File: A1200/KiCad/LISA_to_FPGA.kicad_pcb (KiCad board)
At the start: 4 copper layers, 64 x 37 mm, 30 parts, among them J1 Conn_01x01, J2 Conn_01x40, U1 LM1117-3.3, U2 74LVC162244ADGG, U3 74LVC162244ADGG, U4 LISA, U5 RP2354B

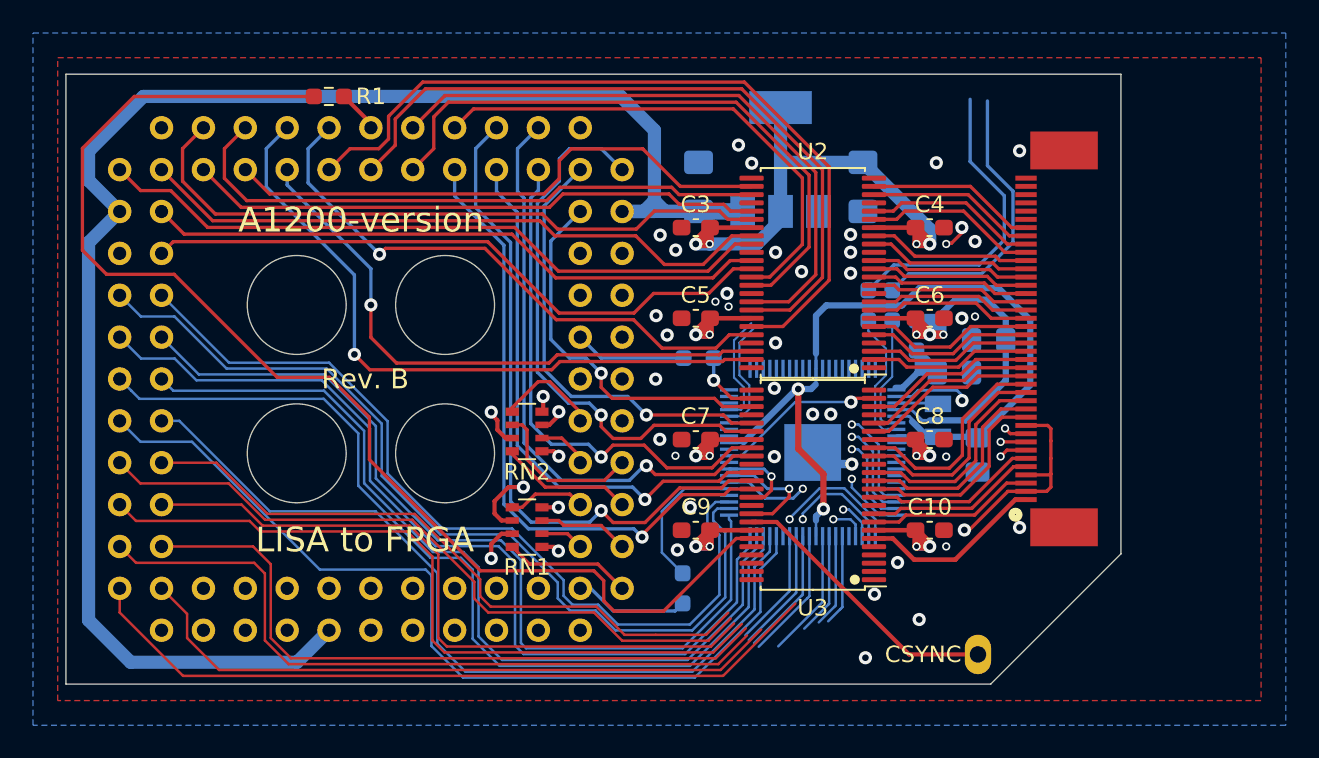
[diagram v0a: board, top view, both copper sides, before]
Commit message: Add 330 Ohm resistor pack RN3 and route D31-D28 to RP2354B
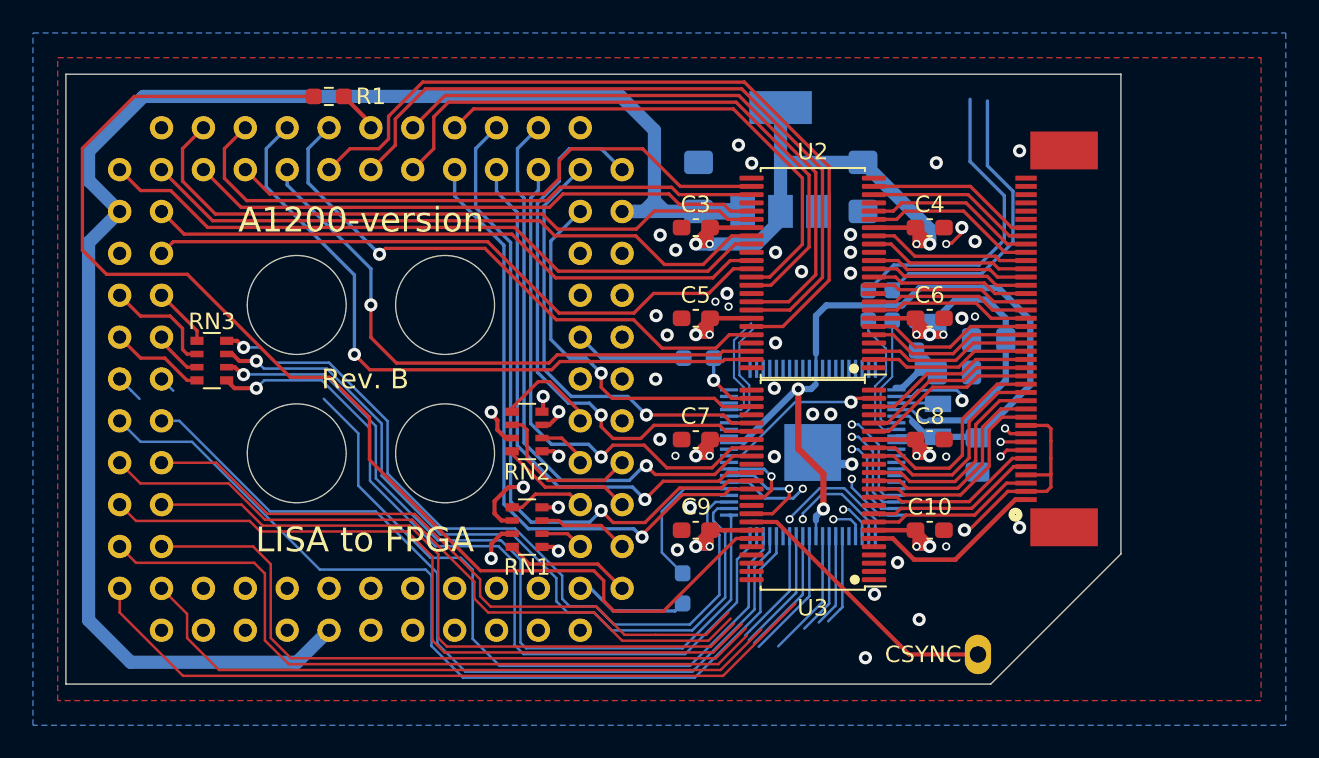
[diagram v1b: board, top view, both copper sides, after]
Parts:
- added RN3: R_Pack04, Resistor_SMD:R_Array_Convex_4x0603, F.Cu at (157.1, 89.3)
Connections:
- net /RGA11 renamed /RGA01
- net /RGA22 renamed /RGA02
- net /RGA33 renamed RGA03
- net /RGA44 renamed /RGA04
- net /RGA55 renamed /RGA05
- net /RGA66 renamed RGA06
- net /RGA77 renamed RGA07
- net /RGA88 renamed /RGA08
- U4 pad 59: D31 -> D031
- U4 pad 60: D30 -> D030
- U4 pad 61: D29 -> D029
- U4 pad 62: D28 -> D028
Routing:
- net D27: track 52.5 -> 1.01 mm
- net D26: track 55.8 -> 44.6 mm
- net D30: track 54.9 -> 47.2 mm, vias 0 -> 1
- net D28: track 55.9 -> 48.7 mm, vias 0 -> 1
- net D030: track 0.00 -> 6.92 mm
- net D028: track 0.00 -> 5.78 mm
- net D31: track 52.2 -> 47.4 mm, vias 0 -> 1
- net D29: track 53.6 -> 49.2 mm, vias 0 -> 1
- net D031: track 0.00 -> 3.65 mm
- net D029: track 0.00 -> 3.07 mm

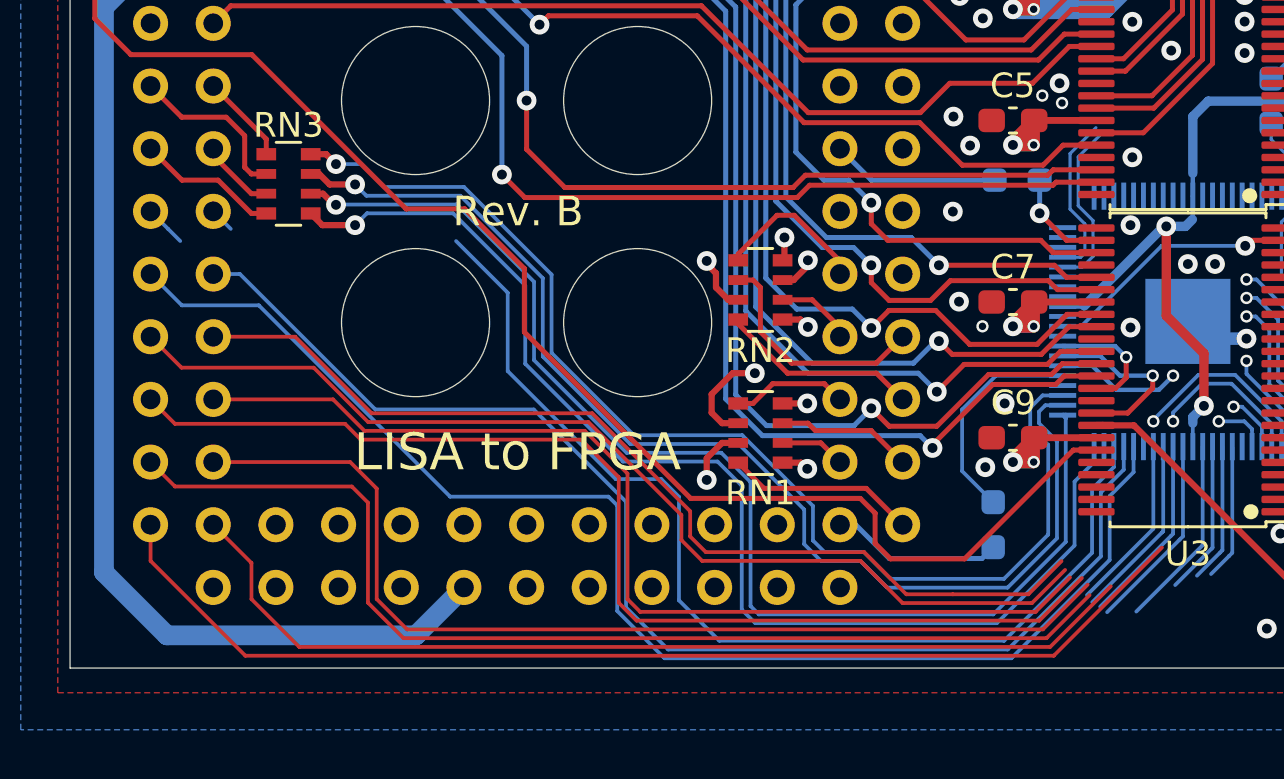
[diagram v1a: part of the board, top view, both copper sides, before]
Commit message: Add RN4 resistor pack and route D27-D24
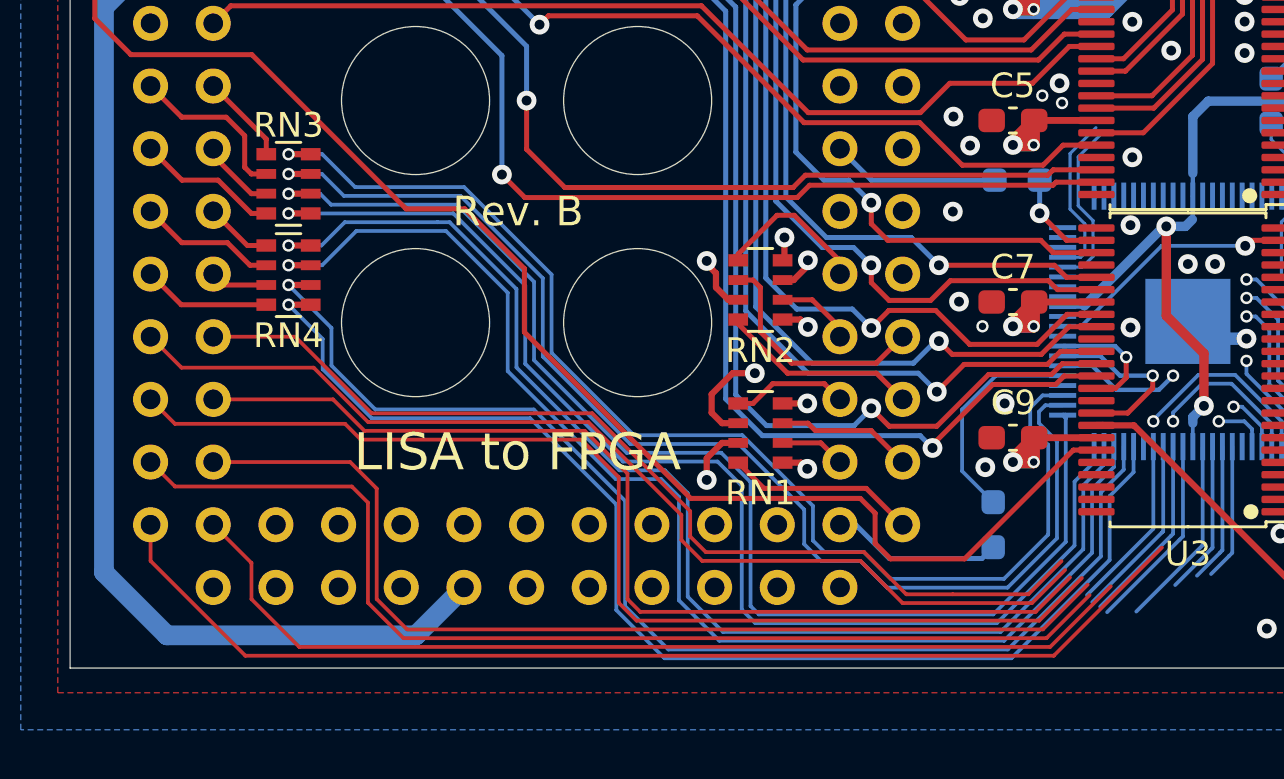
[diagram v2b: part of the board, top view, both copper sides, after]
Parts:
- added RN4: R_Pack04, Resistor_SMD:R_Array_Convex_4x0603, F.Cu at (157.1, 93.0)
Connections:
- net D028 renamed DQ28
- net D029 renamed DQ29
- net D030 renamed DQ30
- net D031 renamed DQ31
- U4 pad 63: D27 -> DQ27
- U4 pad 64: D26 -> DQ26
- U4 pad 65: D25 -> DQ25
- U4 pad 66: D24 -> DQ24
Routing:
- net D27: track 1.01 -> 50.6 mm, vias 0 -> 1
- net D26: track 44.6 -> 51.4 mm, vias 0 -> 1
- net DQ26: track 0.00 -> 5.59 mm
- net DQ24: track 0.00 -> 5.21 mm
- net D24: track 54.5 -> 50.0 mm, vias 0 -> 1
- net DQ27: track 0.00 -> 2.72 mm
- net DQ25: track 0.00 -> 2.33 mm
- net D30: track 47.2 -> 49.0 mm
- net D31: track 47.4 -> 49.2 mm
- net D29: track 49.2 -> 50.9 mm
- net D25: track 51.2 -> 49.7 mm, vias 0 -> 1
- net D28: track 48.7 -> 50.1 mm

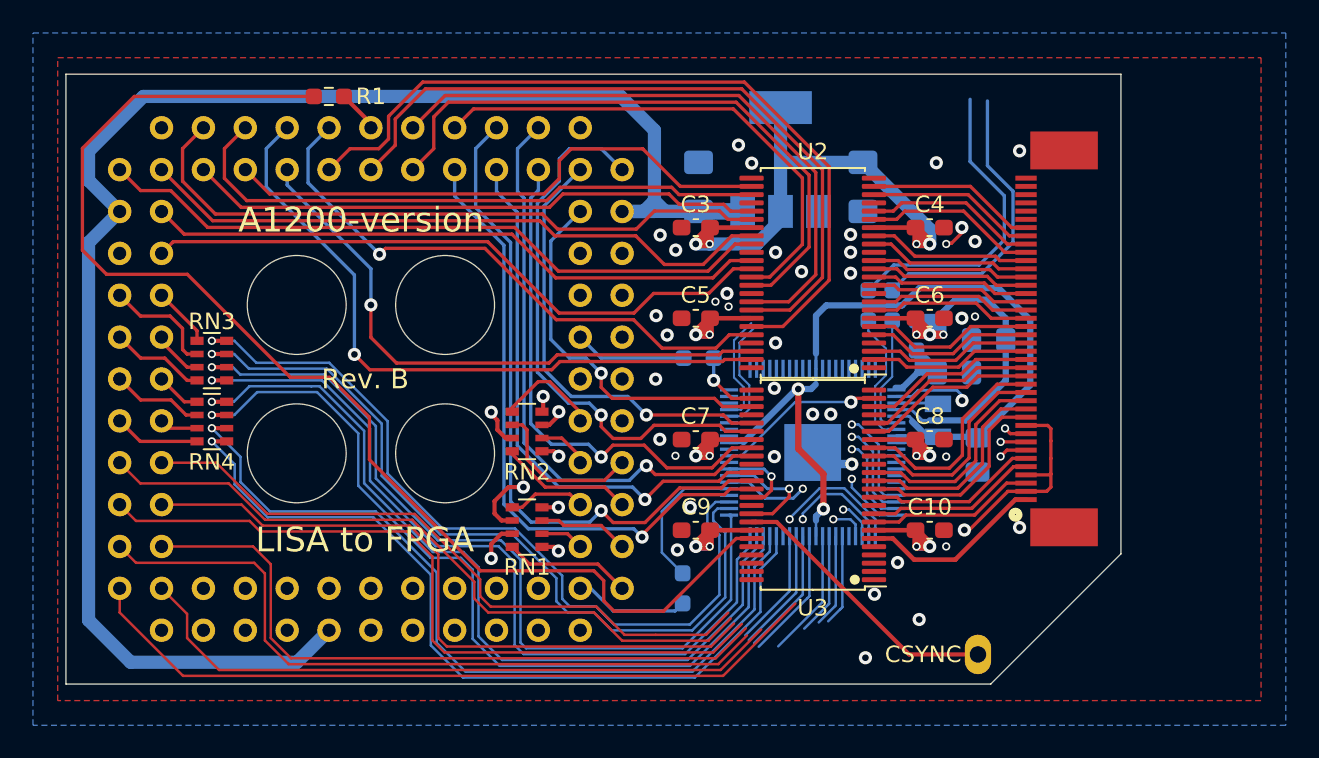
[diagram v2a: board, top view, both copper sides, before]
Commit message: Add RN5 resistor pack and route D23-D20
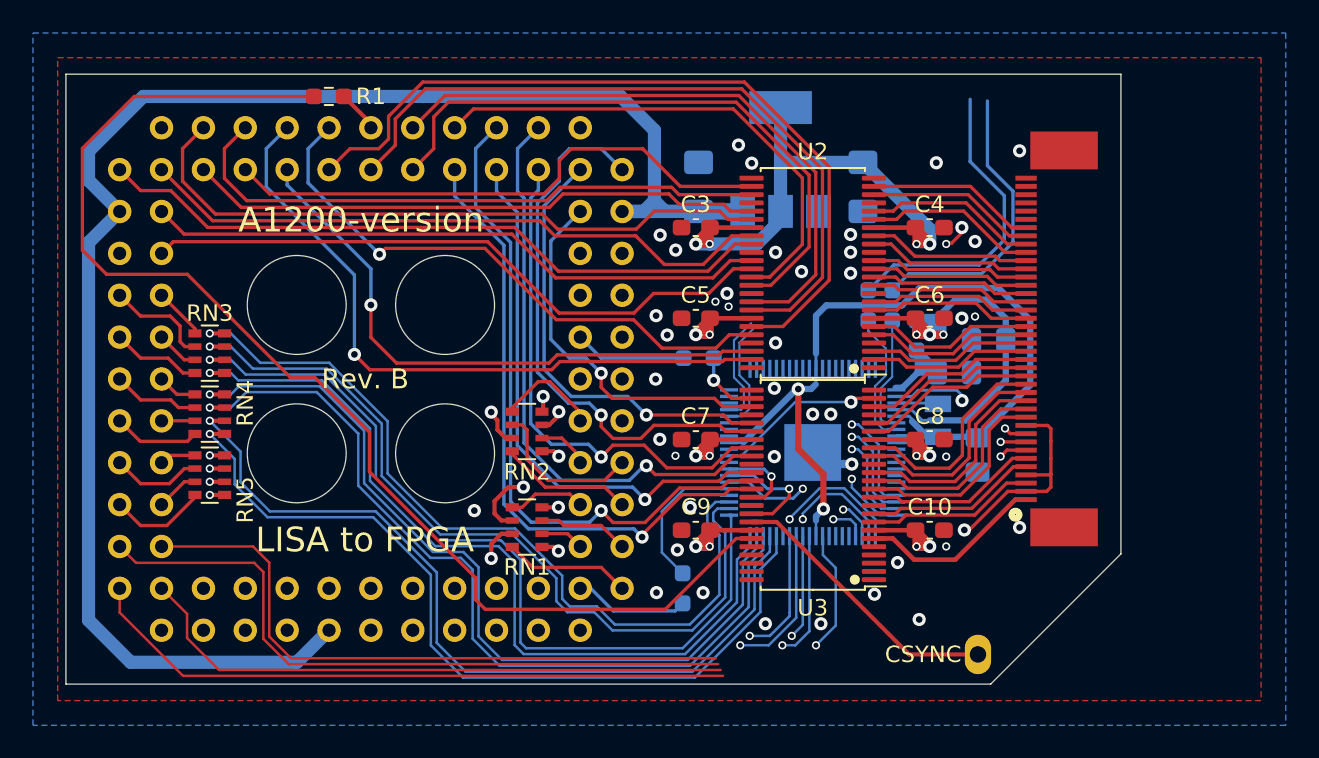
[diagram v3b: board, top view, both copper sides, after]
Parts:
- added RN5: R_Pack04, Resistor_SMD:R_Array_Convex_4x0603, F.Cu at (157.0, 96.3)
- moved RN3 0.47 mm to (157.0, 88.9)
- moved RN4 0.47 mm to (157.0, 92.6)
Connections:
- U4 pad 67: D23 -> DQ23
- U4 pad 68: D22 -> DQ22
- U4 pad 69: D21 -> DQ21
- U4 pad 70: D20 -> DQ20
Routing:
- net D16: track 51.4 -> 39.7 mm
- net D17: track 46.0 -> 36.8 mm
- net D18: track 50.4 -> 41.6 mm
- net DQ20: track 0.00 -> 5.95 mm
- net DQ22: track 0.00 -> 5.47 mm
- net D23: track 47.0 -> 51.2 mm, vias 0 -> 2
- net D21: track 49.6 -> 53.0 mm, vias 0 -> 2
- net D19: track 49.4 -> 46.5 mm, vias 0 -> 1
- net DQ21: track 0.00 -> 2.60 mm
- net DQ23: track 0.00 -> 2.21 mm
- net D22: track 50.2 -> 51.5 mm, vias 0 -> 2
- net D25: track 49.7 -> 50.2 mm
- net DQ31: track 3.65 -> 3.15 mm
- net DQ30: track 6.92 -> 6.41 mm
- net D24: track 50.0 -> 50.5 mm
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
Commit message: Add RN6 resistor pack and route D19-D16, and some silkscreen fixes
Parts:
- added RN6: R_Pack04, Resistor_SMD:R_Array_Convex_4x0603, F.Cu at (157.0, 100.0)
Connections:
- U4 pad 71: D19 -> DQ19
- U4 pad 72: D18 -> DQ18
- U4 pad 73: D17 -> DQ17
- U4 pad 74: D16 -> DQ16
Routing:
- net D17: track 36.8 -> 51.3 mm, vias 0 -> 1
- net D16: track 39.7 -> 51.9 mm, vias 0 -> 1
- net D18: track 41.6 -> 50.3 mm, vias 0 -> 1
- net DQ18: track 0.00 -> 6.39 mm
- net DQ17: track 0.00 -> 5.51 mm
- net DQ16: track 0.00 -> 5.38 mm
- net D19: track 46.5 -> 50.2 mm
- net DQ19: track 0.00 -> 2.87 mm
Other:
- board text added: "Rev. C"
- board text removed: "Rev. B"

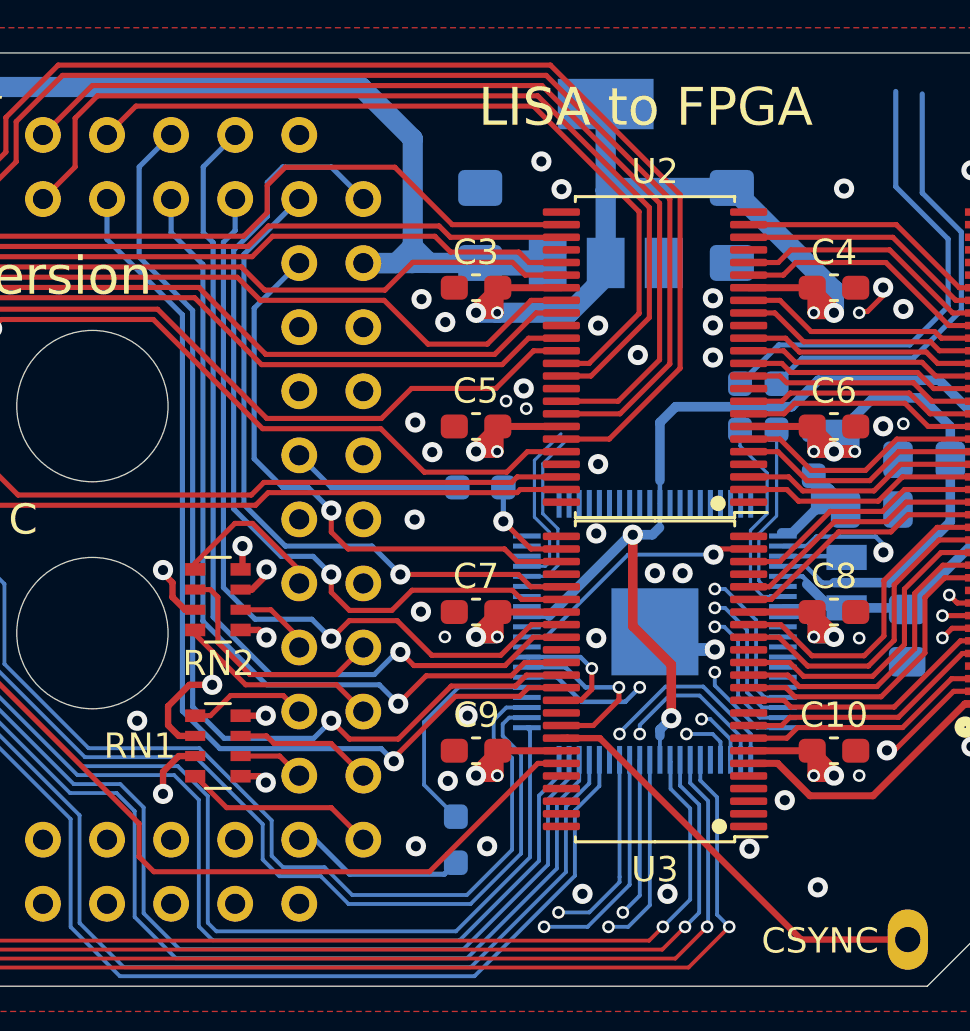
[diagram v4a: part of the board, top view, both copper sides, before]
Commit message: Add decoupling caps for pin 5 and 15 on QFN-80 footprint, fixes of silkscreen on underside of board
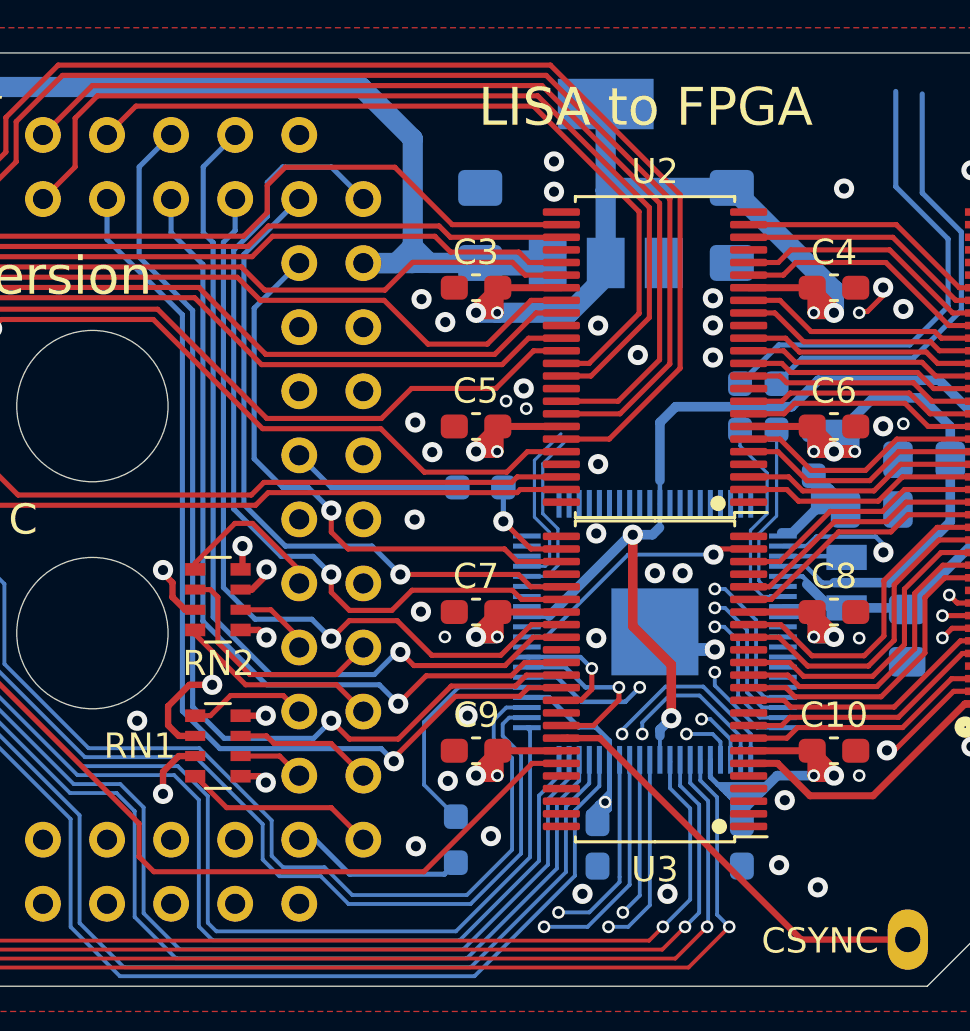
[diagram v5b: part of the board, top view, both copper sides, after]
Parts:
- added C14: 0.1uF, Capacitor_SMD:C_0603_1608Metric_Pad1.08x0.95mm_HandSolder, B.Cu at (191.3, 103.3)
- added C15: 0.1uF, Capacitor_SMD:C_0603_1608Metric_Pad1.08x0.95mm_HandSolder, B.Cu at (197.0, 103.3)
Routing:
- net 3V3: track 122.1 -> 152.7 mm, vias 18 -> 19
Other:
- net class Default: clearance 0.2032 -> 0.2
- rule trace_clearance: 0.2032 -> 0.2
- board text added: "Design by J.Bilander (C) 2023,2024,2026"
- board text removed: "Design by J.Bilander (C) 2023, 2024"
